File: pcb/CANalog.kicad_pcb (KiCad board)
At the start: 2 copper layers, 100 x 45 mm, 84 parts, among them J1 PWR, J3 SPI3, J4 I2C2, J5 STM_PROG, J6 ESP_PROG, J7 AOUT, J8 CAN, Q1 DMP3099L-7, SW1 RESET, SW2 ESP_PROG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

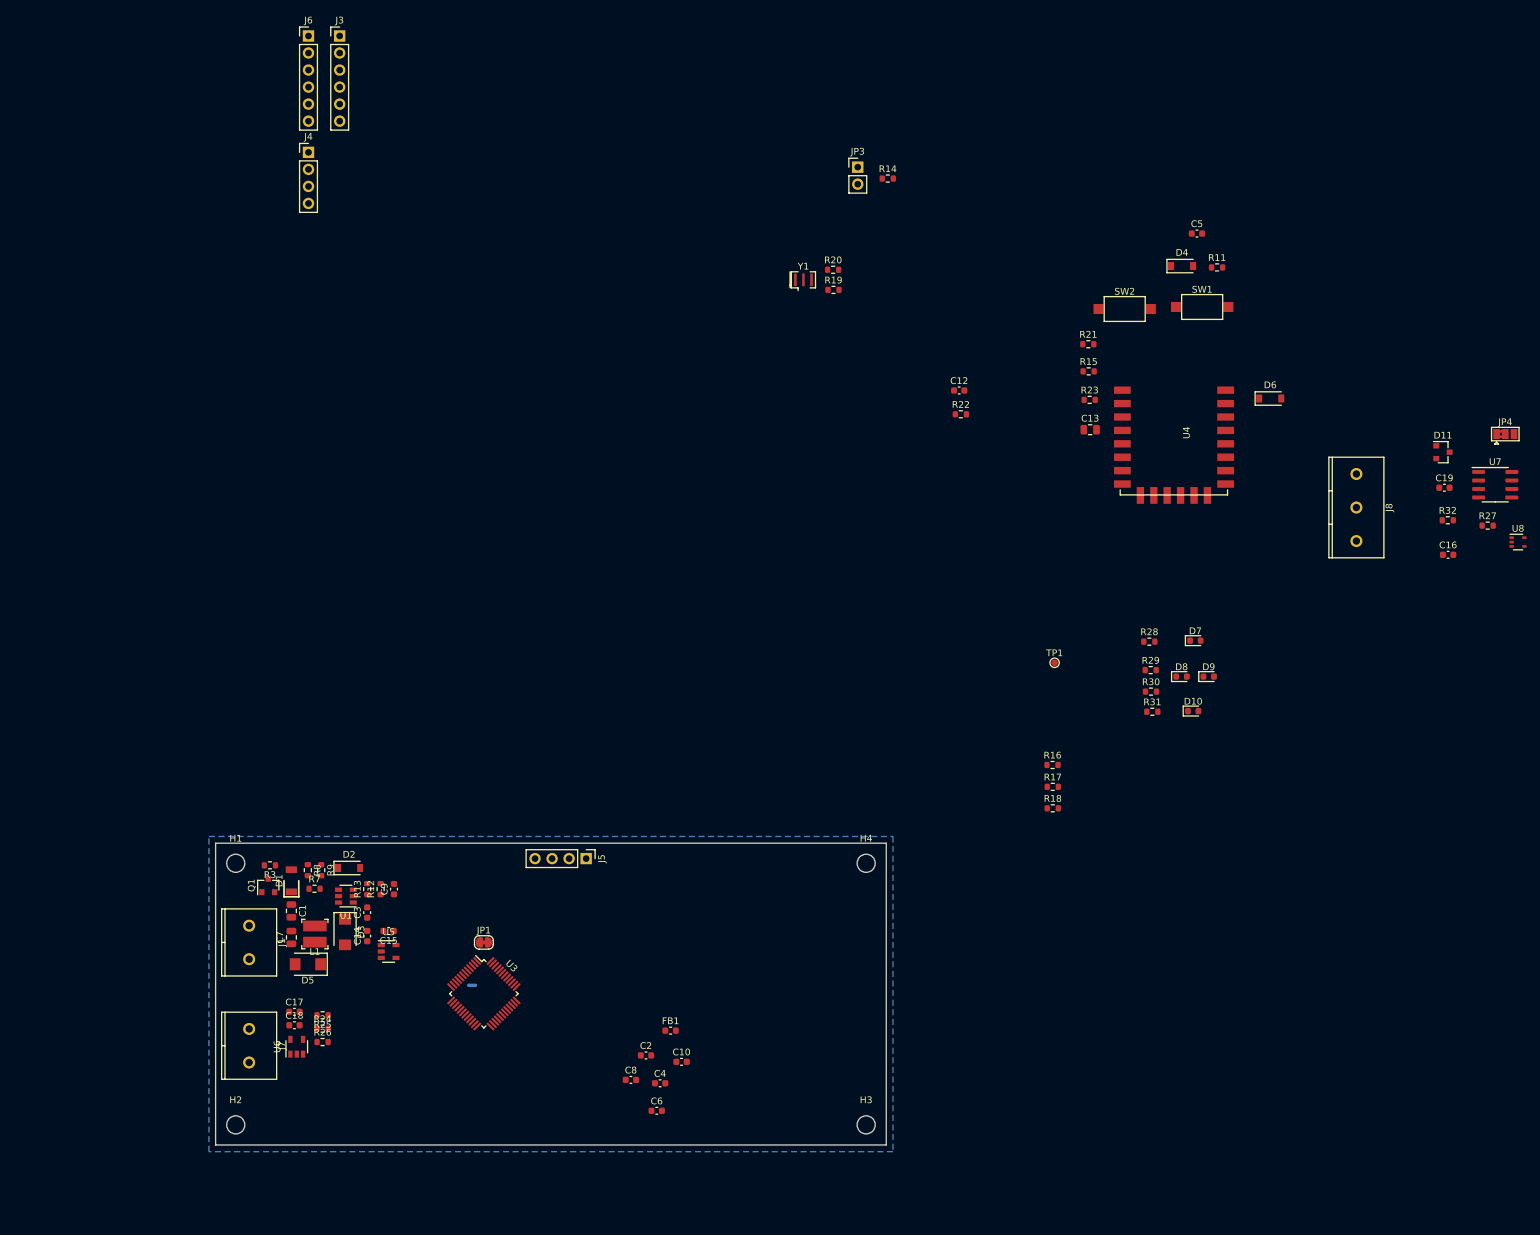
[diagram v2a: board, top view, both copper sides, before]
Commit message: start pcb layout
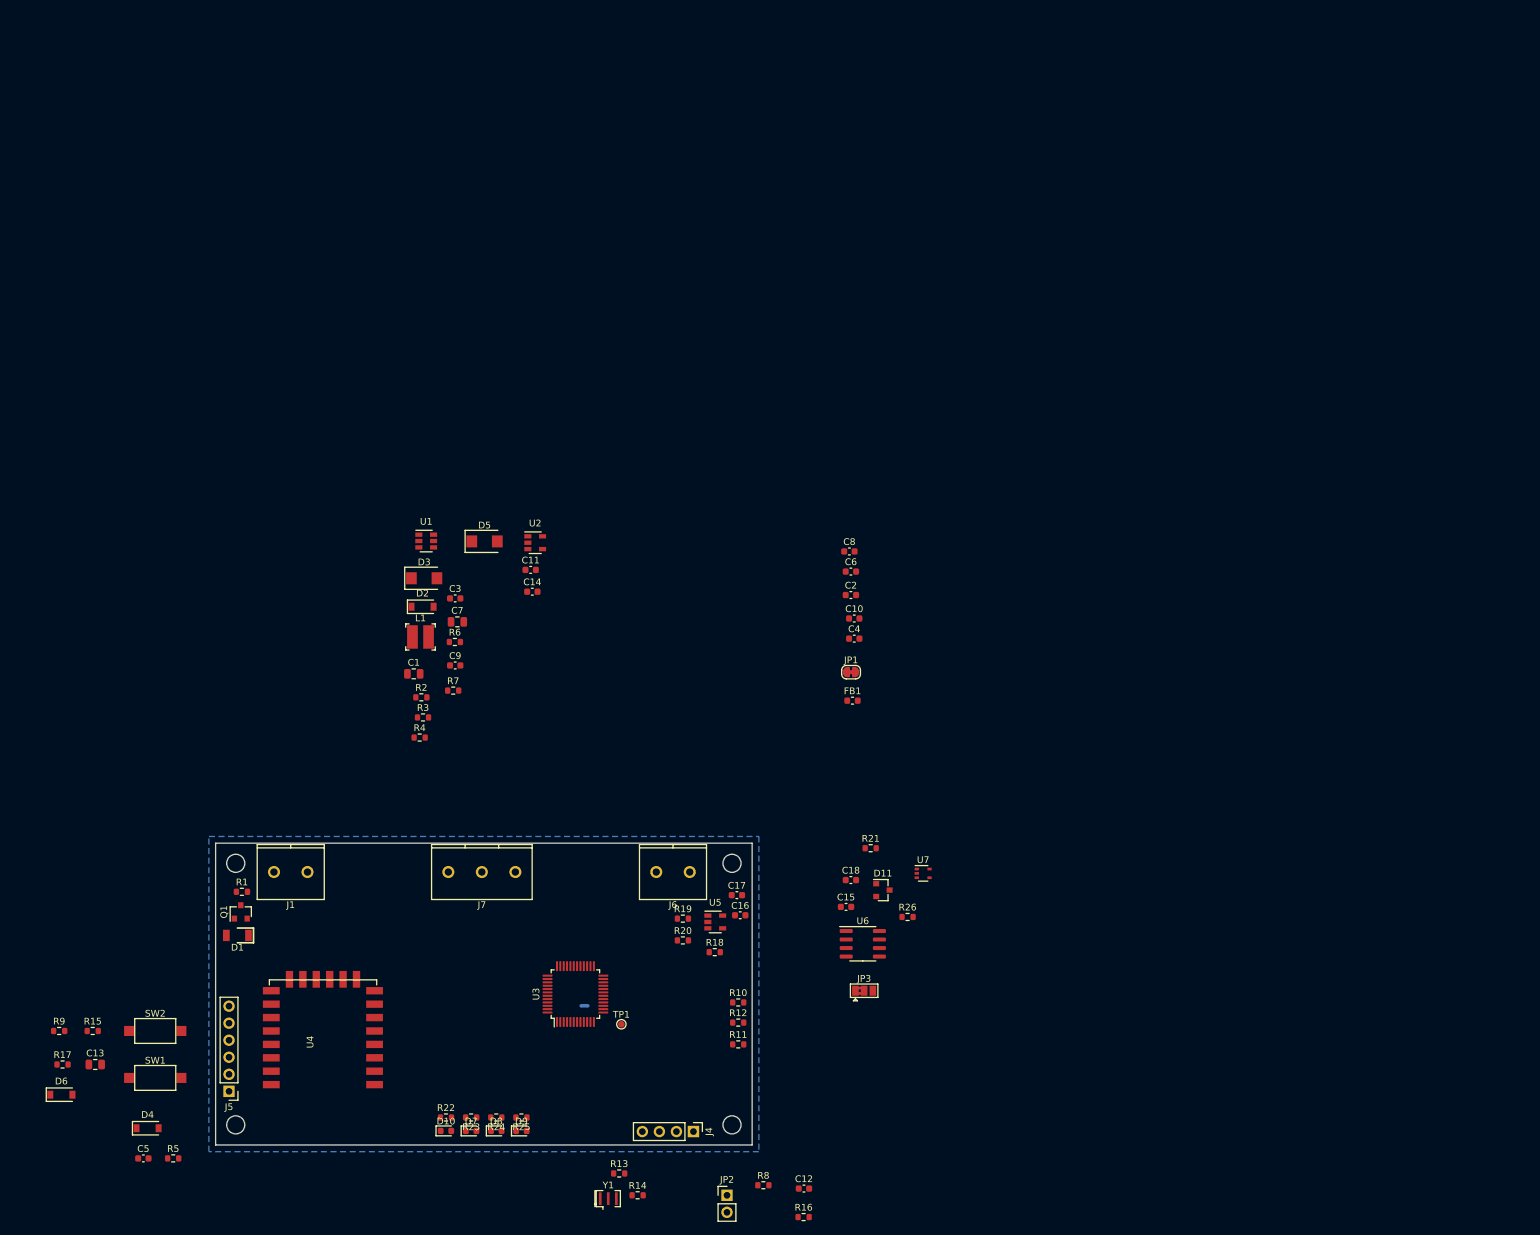
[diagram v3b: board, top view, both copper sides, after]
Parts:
- removed C19: 100nF, Capacitor_SMD:C_0603_1608Metric
- removed J3: SPI3, Connector_PinHeader_2.54mm:PinHeader_1x06_P2.54mm_Vertical
- removed J8: CAN, pl_TerminalBlock:WJ127-5.0-3P
- removed JP4: PSELECT, Jumper:SolderJumper-3_P1.3mm_Bridged2Bar12_Pad1.0x1.5mm
- removed R27: R, Resistor_SMD:R_0603_1608Metric
- removed R28, R29, R30, R31: 1k, Resistor_SMD:R_0603_1608Metric
- removed R32: 120, Resistor_SMD:R_0603_1608Metric
- removed U8: 74AHC1G66, Package_TO_SOT_SMD:SOT-353_SC-70-5
- added C11: 1uF, Capacitor_SMD:C_0603_1608Metric, F.Cu at (72.0, 99.2)
- added JP2: BOOT0, Connector_PinHeader_2.54mm:PinHeader_1x02_P2.54mm_Vertical, F.Cu at (101.2, 192.5)
- added R1: 10k, Resistor_SMD:R_0603_1608Metric, F.Cu at (28.9, 147.2)
- added R10: 1k, Resistor_SMD:R_0603_1608Metric, F.Cu at (102.9, 163.8)
- added R2: 120k, Resistor_SMD:R_0603_1608Metric, F.Cu at (55.7, 118.2)
- added R4: 12k, Resistor_SMD:R_0603_1608Metric, F.Cu at (55.4, 124.2)
- added R5: 10k, Resistor_SMD:R_0603_1608Metric, F.Cu at (18.7, 187.0)
- added R6: 124k, Resistor_SMD:R_0603_1608Metric, F.Cu at (60.7, 110.0)
- added U2: MIC5504-3.3YM5, Package_TO_SOT_SMD:SOT-23-5, F.Cu at (72.7, 95.2)
- C15, C18: value 1uF -> 100nF
- C17: value 100nF -> 1uF
- J4: value I2C2 -> STM_PROG
- J5: value STM_PROG -> ESP_PROG; footprint Connector_PinHeader_2.54mm:PinHeader_1x04_P2.54mm_Vertical -> Connector_PinHeader_2.54mm:PinHeader_1x06_P2.54mm_Vertical
- J6: value ESP_PROG -> AOUT; footprint Connector_PinHeader_2.54mm:PinHeader_1x06_P2.54mm_Vertical -> pl_TerminalBlock:WJ127-5.0-2P
- J7: value AOUT -> CAN; footprint pl_TerminalBlock:WJ127-5.0-2P -> pl_TerminalBlock:WJ127-5.0-3P
- JP3: value BOOT0 -> PSELECT; footprint Connector_PinHeader_2.54mm:PinHeader_1x02_P2.54mm_Vertical -> Jumper:SolderJumper-3_P1.3mm_Bridged2Bar12_Pad1.0x1.5mm
- R11, R22, R23: value 10k -> 1k
- R12: value 124k -> 1k
- R13: value 20.5k -> R
- R14: value 1k -> R
- R16, R17: value 1k -> 10k
- R18: value 1k -> 120k
- R19: value R -> 12k
- R20: value R -> 68k
- R21: value 10k -> R
- R24: value 120k -> 1k
- R25: value 12k -> 1k
- R26: value 68k -> 120
- R3: value 10k -> 20k
- R7: value 120k -> 20.5k
- R8: value 20k -> 1k
- R9: value 12k -> 10k
- U5: value MIC5504-3.3YM5 -> OPA330xxDBV
- U6: value OPA330xxDBV -> SN65HVD230; footprint Package_TO_SOT_SMD:SOT-23-5 -> Package_SO:SOIC-8_3.9x4.9mm_P1.27mm
- U7: value SN65HVD230 -> 74AHC1G66; footprint Package_SO:SOIC-8_3.9x4.9mm_P1.27mm -> Package_TO_SOT_SMD:SOT-353_SC-70-5
- moved C5 209.0 mm to (14.2, 187.0)
- moved D6 208.0 mm to (2.00, 177.5)
- moved D4 200.8 mm to (14.8, 182.5)
- moved SW1 193.9 mm to (16.0, 175.0)
- moved SW2 180.2 mm to (16.0, 168.0)
- moved R15 178.1 mm to (6.67, 168.0)
- moved C13 176.0 mm to (7.05, 173.0)
- moved J4 156.9 mm to (96.2, 183.0), turned to 270 degrees
- moved R14 156.1 mm to (87.9, 192.5)
- moved R17 153.3 mm to (2.17, 173.0)
- moved U4 153.2 mm to (48.0, 176.0), turned to 180 degrees
- moved R23 141.3 mm to (63.1, 180.9), turned to 180 degrees
- moved Y1 140.1 mm to (83.5, 193.0)
- moved J6 137.0 mm to (95.7, 144.3), turned to 180 degrees
- moved R11 136.1 mm to (102.9, 170.0)
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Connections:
- C14 pad 1: +5V -> +3V3
- C15 pad 1: +3V3 -> GND
- C15 pad 2: GND -> /OA_PWR
- C16 pad 1: GND -> +5V
- C16 pad 2: /OA_PWR -> GNDA
- C18 pad 1: +5V -> GND
- C18 pad 2: GNDA -> +5V
- J4 pad 1: +5V -> Net-(J4-Pad1)
- J4 pad 2: /I2C_SCL -> /SWDIO
- J4 pad 3: /I2C_SDA -> /SWCLK
- J5 pad 2: /SWDIO -> /TXD
- J5 pad 3: /SWCLK -> Net-(D6-Pad1)
- J5 pad 4: GND -> Net-(J5-Pad4)
- J6 pad 2: /TXD -> GNDA
- J7 pad 1: Net-(J7-Pad1) -> /CANH
- J7 pad 2: GNDA -> /CANL
- JP3 pad 1: Net-(JP3-Pad1) -> +3V3
- JP3 pad 2: /BOOT0 -> /OA_PWR
- R11 pad 1: +3V3 -> GND
- R11 pad 2: ESP_RESET -> V_B1
- R12 pad 1: /5V5 -> GND
- R12 pad 2: Net-(C9-Pad2) -> V_B0
- R13 pad 1: GND -> /XIN
- R13 pad 2: Net-(C9-Pad2) -> Net-(R13-Pad2)
- R14 pad 1: +3V3 -> /XOUT
- R14 pad 2: Net-(JP3-Pad1) -> Net-(R14-Pad2)
- R15 pad 2: GPIO2 -> CH_PD
- R16 pad 1: GND -> +3V3
- R16 pad 2: V_B2 -> STM_RESET
- R17 pad 1: GND -> STM_CS
- R17 pad 2: V_B1 -> GND
- R18 pad 1: GND -> Net-(R18-Pad1)
- R18 pad 2: V_B0 -> Net-(R18-Pad2)
- R19 pad 1: /XIN -> Net-(R18-Pad2)
- R19 pad 2: Net-(R19-Pad2) -> GNDA
- R20 pad 1: /XOUT -> Net-(J6-Pad1)
- R20 pad 2: Net-(R20-Pad2) -> Net-(R18-Pad1)
- R21 pad 1: +3V3 -> Net-(R21-Pad1)
- R21 pad 2: CH_PD -> CAN_RS
- R22 pad 1: +3V3 -> Net-(D10-Pad1)
- R22 pad 2: STM_RESET -> GPIO0
- R23 pad 1: STM_CS -> GND
- R23 pad 2: GND -> Net-(D7-Pad1)
- R24 pad 1: Net-(R24-Pad1) -> GND
- R24 pad 2: Net-(R24-Pad2) -> Net-(D8-Pad1)
- R25 pad 1: Net-(R24-Pad2) -> GND
- R25 pad 2: GNDA -> Net-(D9-Pad1)
- R26 pad 1: Net-(J7-Pad1) -> /CANH
- R26 pad 2: Net-(R24-Pad1) -> Net-(R26-Pad2)
- R3 pad 1: Net-(D1-Pad2) -> Net-(R3-Pad1)
- R3 pad 2: GND -> Net-(D2-Pad1)
- R7 pad 1: Net-(D2-Pad1) -> GND
- R7 pad 2: /Vin -> Net-(C9-Pad2)
- R8 pad 1: Net-(R8-Pad1) -> +3V3
- R8 pad 2: Net-(D2-Pad1) -> Net-(JP2-Pad1)
- R9 pad 1: GND -> +3V3
- R9 pad 2: Net-(R8-Pad1) -> GPIO2
- U3 pad 30: /I2C_SCL -> Net-(U3-Pad30)
- U3 pad 31: /I2C_SDA -> Net-(U3-Pad31)
- U3 pad 38: /SPI3_CS -> Net-(U3-Pad38)
- U3 pad 39: /SPI3_SCK -> Net-(U3-Pad39)
- U3 pad 40: /SPI3_MISO -> Net-(U3-Pad40)
- U3 pad 41: /SPI3_MOSI -> Net-(U3-Pad41)
- U5 pad 1: +5V -> Net-(J6-Pad1)
- U5 pad 2: GND -> GNDA
- U5 pad 3: +5V -> DAC
- U5 pad 4: Net-(U5-Pad4) -> Net-(R18-Pad1)
- U5 pad 5: +3V3 -> +5V
- U6 pad 1: Net-(J7-Pad1) -> CAN_TX
- U6 pad 2: GNDA -> GND
- U6 pad 3: DAC -> /OA_PWR
- U6 pad 4: Net-(R24-Pad1) -> CAN_RX
- U6 pad 5: +5V -> Net-(U6-Pad5)
- U7 pad 1: CAN_TX -> /CANL
- U7 pad 2: GND -> Net-(R26-Pad2)
- U7 pad 3: /OA_PWR -> GND
- U7 pad 4: CAN_RX -> CAN_TERM
- U7 pad 5: Net-(U7-Pad5) -> +5V
- Y1 pad 1: Net-(R19-Pad2) -> Net-(R13-Pad2)
- Y1 pad 3: Net-(R20-Pad2) -> Net-(R14-Pad2)
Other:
- board size 100 x 45 mm -> 80 x 45 mm

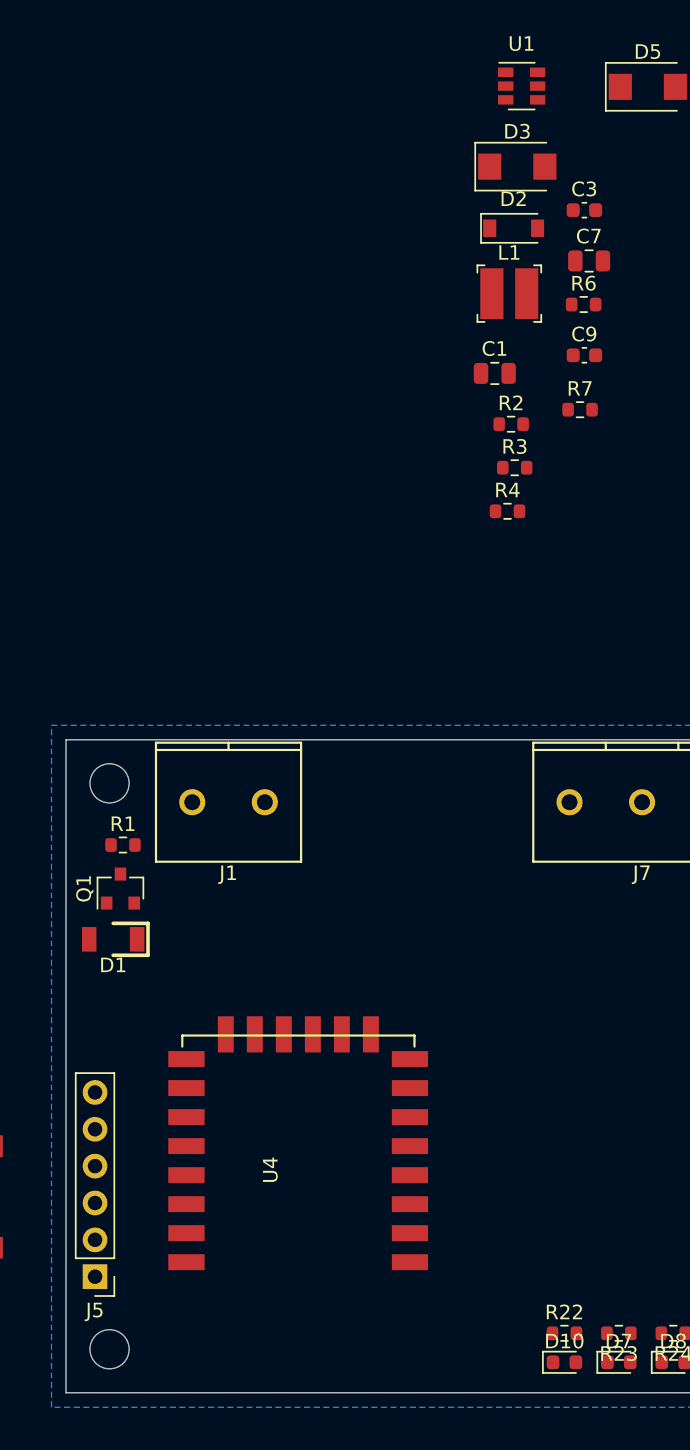
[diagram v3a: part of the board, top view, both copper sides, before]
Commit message: start power supply layout
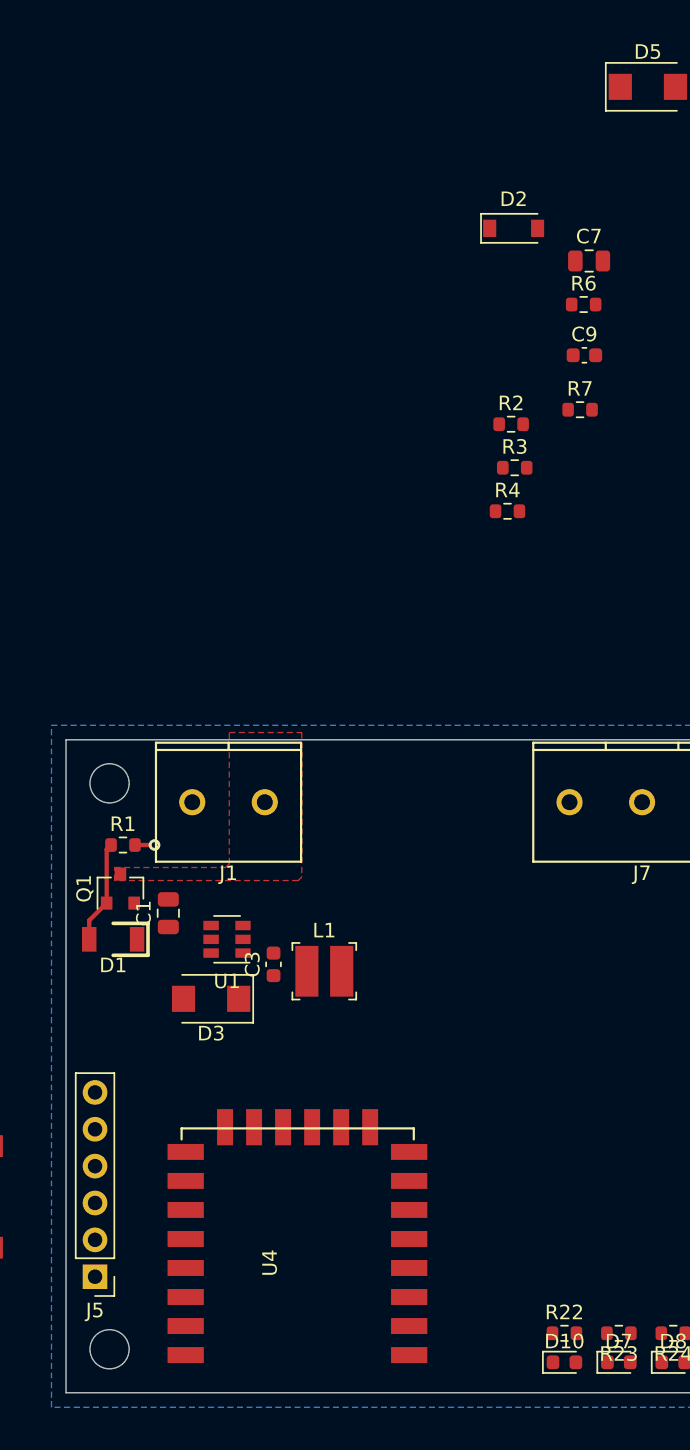
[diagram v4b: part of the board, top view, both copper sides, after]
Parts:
- moved U1 62.2 mm to (36.1, 153.8), turned to 180 degrees
- moved D3 61.1 mm to (35.0, 157.8), turned to 180 degrees
- moved C3 56.2 mm to (39.3, 155.5), turned to 90 degrees
- moved L1 48.4 mm to (42.8, 155.9)
- moved C1 43.5 mm to (32.0, 151.9), turned to 90 degrees
- moved U4 6.40 mm to (48.0, 182.4)
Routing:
- net Net-(D1-Pad2): track 0.00 -> 7.12 mm
- net GND: track 0.00 -> 1.35 mm, vias 0 -> 1
- added copper zone on F.Cu, net Net-(J1-Pad1)
